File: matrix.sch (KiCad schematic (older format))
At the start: 6 parts

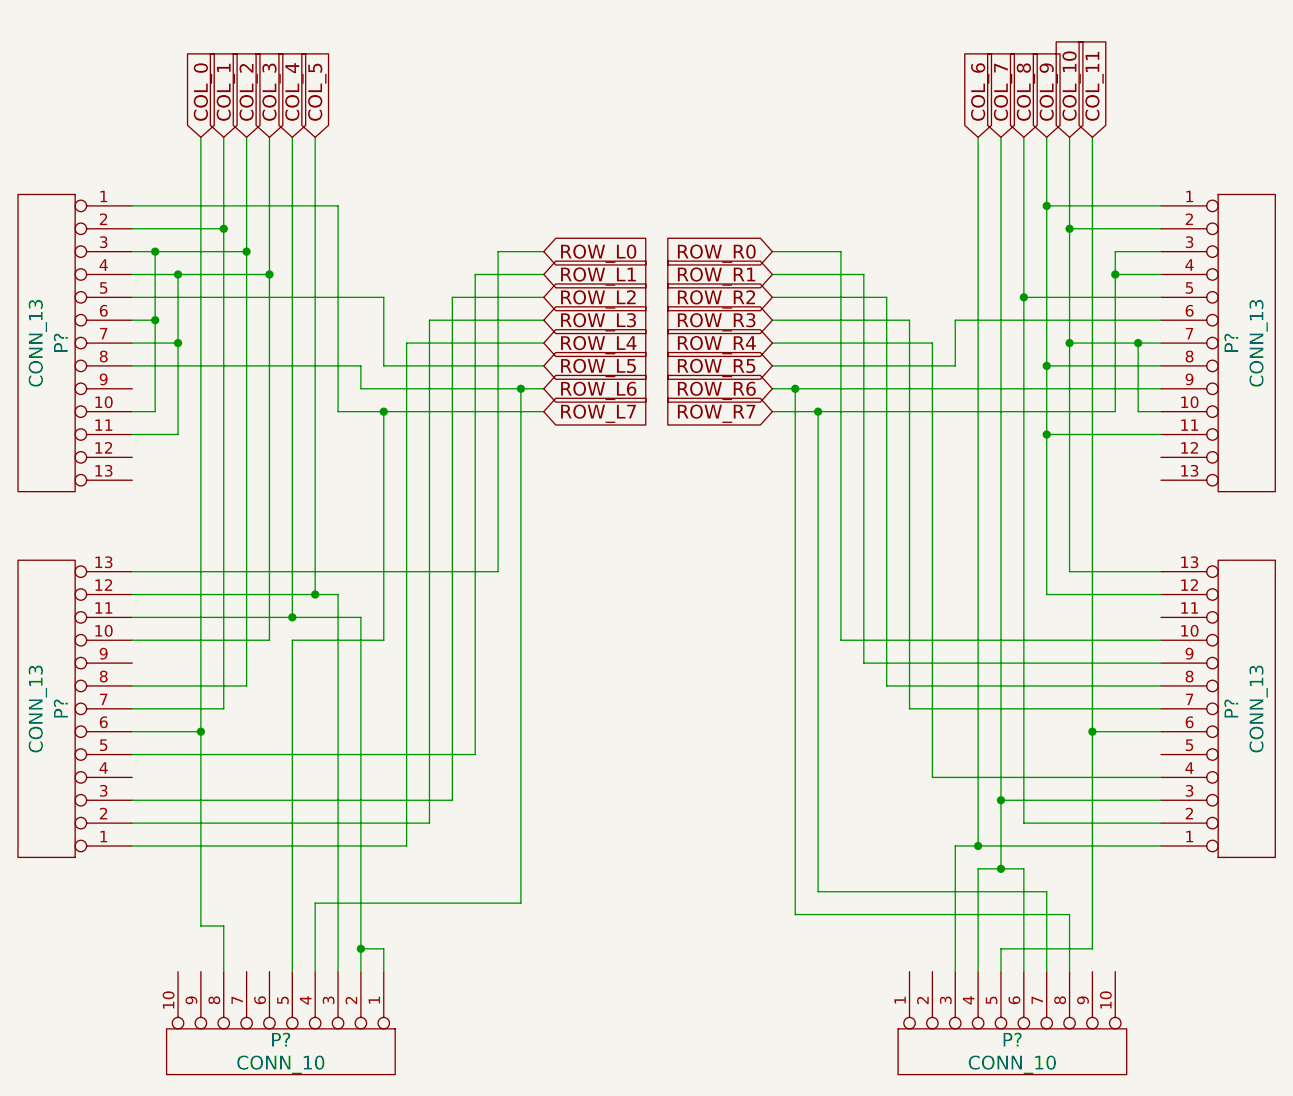
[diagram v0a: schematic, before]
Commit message: Add annotations to parts
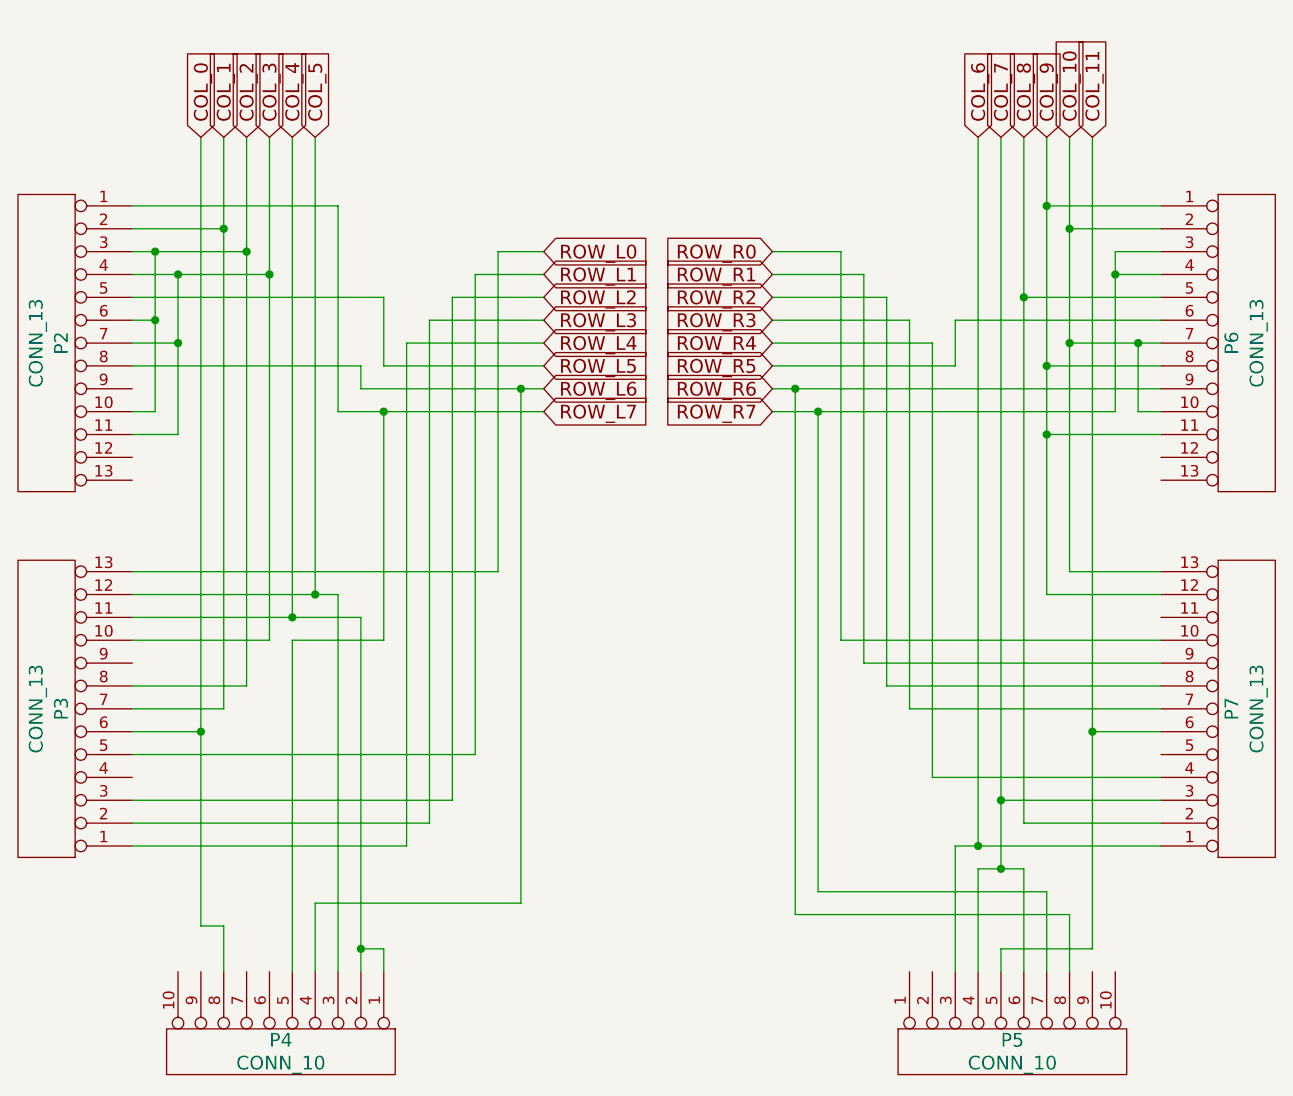
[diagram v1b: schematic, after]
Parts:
- gave numbers to parts that had none: 6
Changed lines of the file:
@@
 $EndDescr
 $Comp
-L CONN_13 P?
+L CONN_13 P3
 U 1 1 54E4BDF3
 P 1900 4000
-F 0 "P?" V 1860 4000 60  0000 C CNN
+F 0 "P3" V 1860 4000 60  0000 C CNN
 F 1 "CONN_13" V 1970 4000 60  0000 C CNN
 F 2 "" H 1900 4000 60  0000 C CNN
@@
 $EndComp
 $Comp
-L CONN_13 P?
+L CONN_13 P2
 U 1 1 54E4BDFA
 P 1900 2400
-F 0 "P?" V 1860 2400 60  0000 C CNN
+F 0 "P2" V 1860 2400 60  0000 C CNN
 F 1 "CONN_13" V 1970 2400 60  0000 C CNN
 F 2 "" H 1900 2400 60  0000 C CNN
@@
 $EndComp
 $Comp
-L CONN_13 P?
+L CONN_13 P6
 U 1 1 54E4BE01
 P 7100 2400
-F 0 "P?" V 7060 2400 60  0000 C CNN
+F 0 "P6" V 7060 2400 60  0000 C CNN
 F 1 "CONN_13" V 7170 2400 60  0000 C CNN
 F 2 "" H 7100 2400 60  0000 C CNN
@@
 $EndComp
 $Comp
-L CONN_13 P?
+L CONN_13 P7
 U 1 1 54E4BE08
 P 7100 4000
-F 0 "P?" V 7060 4000 60  0000 C CNN
+F 0 "P7" V 7060 4000 60  0000 C CNN
 F 1 "CONN_13" V 7170 4000 60  0000 C CNN
 F 2 "" H 7100 4000 60  0000 C CNN
@@
 $EndComp
 $Comp
-L CONN_10 P?
+L CONN_10 P5
 U 1 1 54E4BE0F
 P 6100 5500
-F 0 "P?" V 6050 5500 60  0000 C CNN
+F 0 "P5" V 6050 5500 60  0000 C CNN
 F 1 "CONN_10" V 6150 5500 60  0000 C CNN
 F 2 "" H 6100 5500 60  0000 C CNN
@@
 $EndComp
 $Comp
-L CONN_10 P?
+L CONN_10 P4
 U 1 1 54E4BE16
 P 2900 5500
-F 0 "P?" V 2850 5500 60  0000 C CNN
+F 0 "P4" V 2850 5500 60  0000 C CNN
 F 1 "CONN_10" V 2950 5500 60  0000 C CNN
 F 2 "" H 2900 5500 60  0000 C CNN

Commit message: WT12 breakout headers are now in place
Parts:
- P2, P7: footprint (none) -> replacement_kinesis_controller:Molex_FFC_13_mirror
- P3, P6: footprint (none) -> replacement_kinesis_controller:Molex_FFC_13
- P4, P5: footprint (none) -> replacement_kinesis_controller:Pin_Header_Staggered_Straight_1x10
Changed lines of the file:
@@
 F 0 "P3" V 1860 4000 60  0000 C CNN
 F 1 "CONN_13" V 1970 4000 60  0000 C CNN
-F 2 "" H 1900 4000 60  0000 C CNN
+F 2 "replacement_kinesis_controller:Molex_FFC_13" H 1900 4000 60  0001 C CNN
 F 3 "" H 1900 4000 60  0000 C CNN
 	1    1900 4000
@@
 F 0 "P2" V 1860 2400 60  0000 C CNN
 F 1 "CONN_13" V 1970 2400 60  0000 C CNN
-F 2 "" H 1900 2400 60  0000 C CNN
+F 2 "replacement_kinesis_controller:Molex_FFC_13_mirror" H 1900 2400 60  0001 C CNN
 F 3 "" H 1900 2400 60  0000 C CNN
 	1    1900 2400
@@
 F 0 "P6" V 7060 2400 60  0000 C CNN
 F 1 "CONN_13" V 7170 2400 60  0000 C CNN
-F 2 "" H 7100 2400 60  0000 C CNN
+F 2 "replacement_kinesis_controller:Molex_FFC_13" H 7100 2400 60  0001 C CNN
 F 3 "" H 7100 2400 60  0000 C CNN
 	1    7100 2400
@@
 F 0 "P7" V 7060 4000 60  0000 C CNN
 F 1 "CONN_13" V 7170 4000 60  0000 C CNN
-F 2 "" H 7100 4000 60  0000 C CNN
+F 2 "replacement_kinesis_controller:Molex_FFC_13_mirror" H 7100 4000 60  0001 C CNN
 F 3 "" H 7100 4000 60  0000 C CNN
 	1    7100 4000
@@
 F 0 "P5" V 6050 5500 60  0000 C CNN
 F 1 "CONN_10" V 6150 5500 60  0000 C CNN
-F 2 "" H 6100 5500 60  0000 C CNN
+F 2 "replacement_kinesis_controller:Pin_Header_Staggered_Straight_1x10" H 6100 5500 60  0001 C CNN
 F 3 "" H 6100 5500 60  0000 C CNN
 	1    6100 5500
@@
 F 0 "P4" V 2850 5500 60  0000 C CNN
 F 1 "CONN_10" V 2950 5500 60  0000 C CNN
-F 2 "" H 2900 5500 60  0000 C CNN
+F 2 "replacement_kinesis_controller:Pin_Header_Staggered_Straight_1x10" H 2900 5500 60  0001 C CNN
 F 3 "" H 2900 5500 60  0000 C CNN
 	1    2900 5500
